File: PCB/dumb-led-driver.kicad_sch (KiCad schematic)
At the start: 17 parts, among them J1 ProgConn-SOICBite, J2 12V PWR, SW1 RESET, SW2 FLASH, U2 ESP-12F

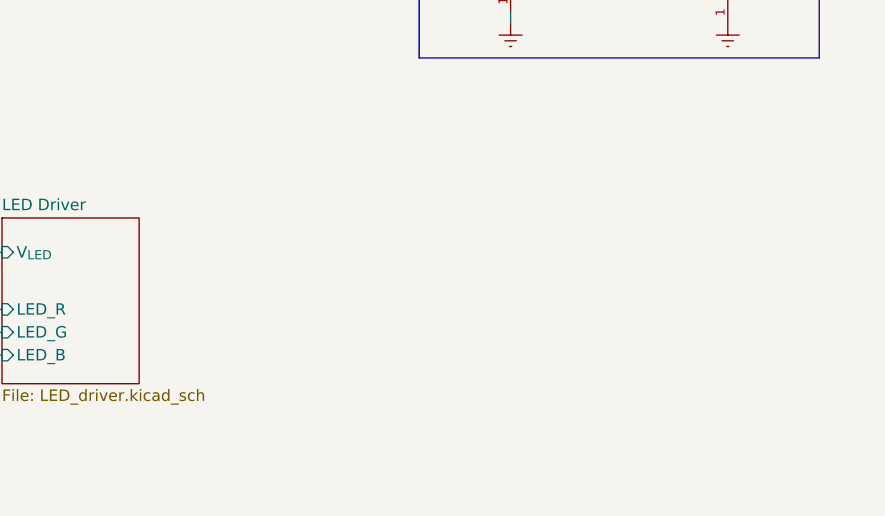
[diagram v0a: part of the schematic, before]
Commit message: fuse added to schematic. began board re-layout
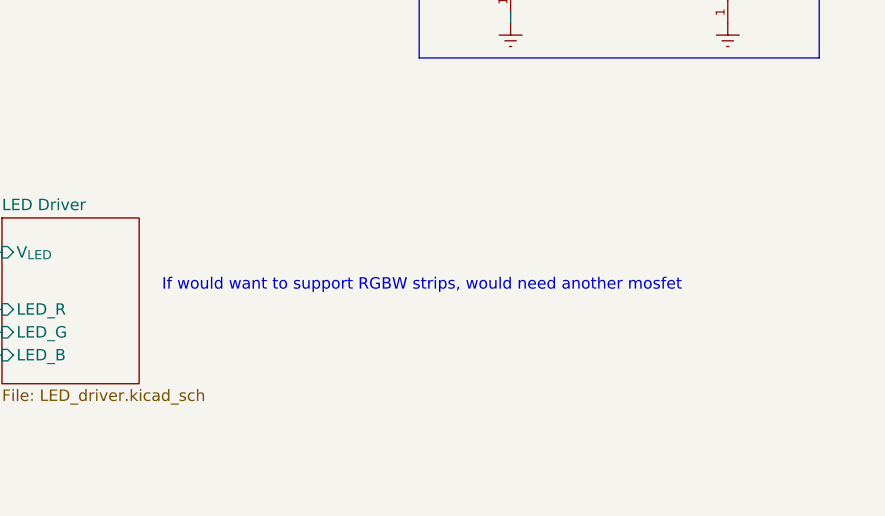
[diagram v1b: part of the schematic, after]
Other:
- note added: "If would want to support RGBW strips, would need another mosfet"
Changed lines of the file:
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@@
     (fill (type none))
+  )
+  (text "If would want to support RGBW strips, would need another mosfet"
+    (at 203.2 114.3 0)
+    (effects (font (size 1.27 1.27)) (justify left bottom))
   )
   (text "Buttons\n" (at 249.555 53.975 0)

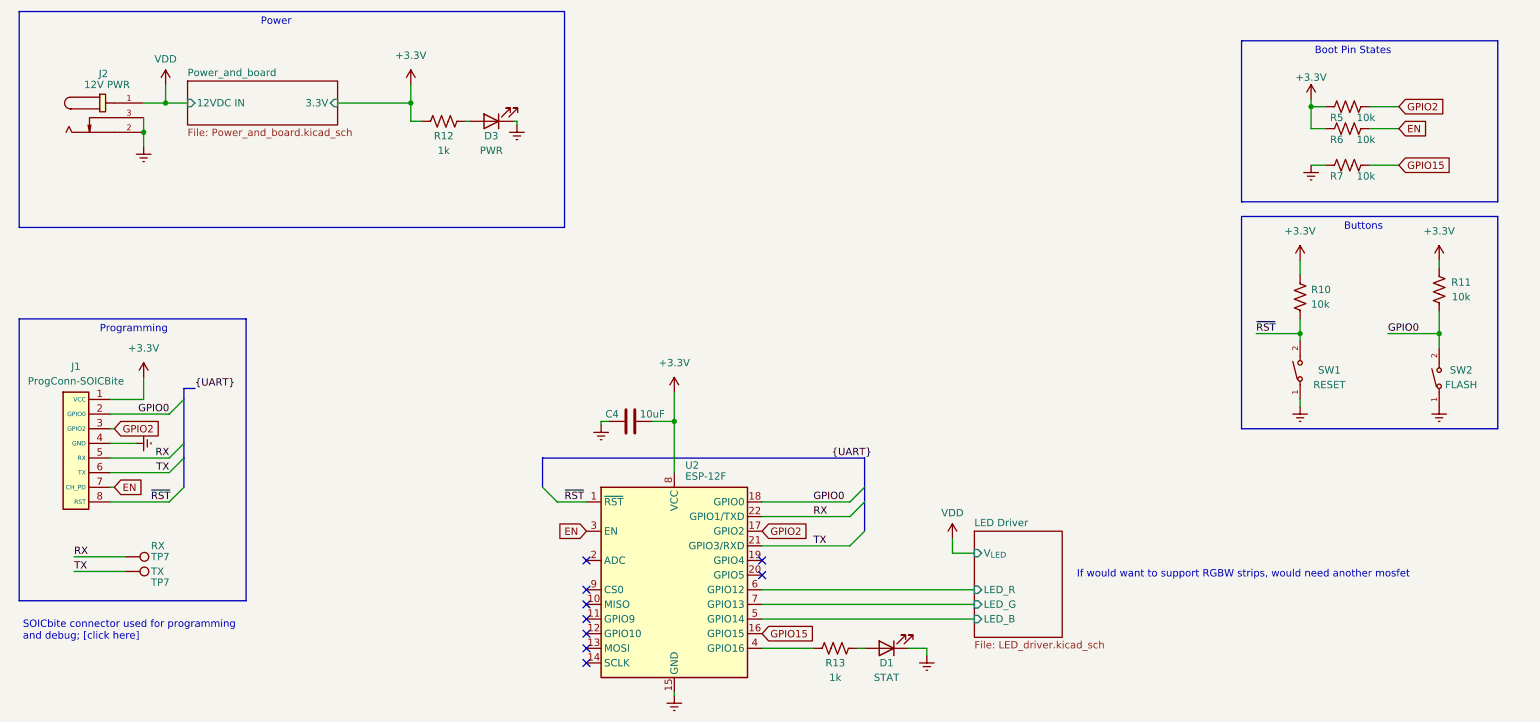
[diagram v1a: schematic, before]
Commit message: began rev2 of layout. board size will have to be increased
- will need to make compomises regarding I/O, wont be able to make both power in and out fit on same short side :(
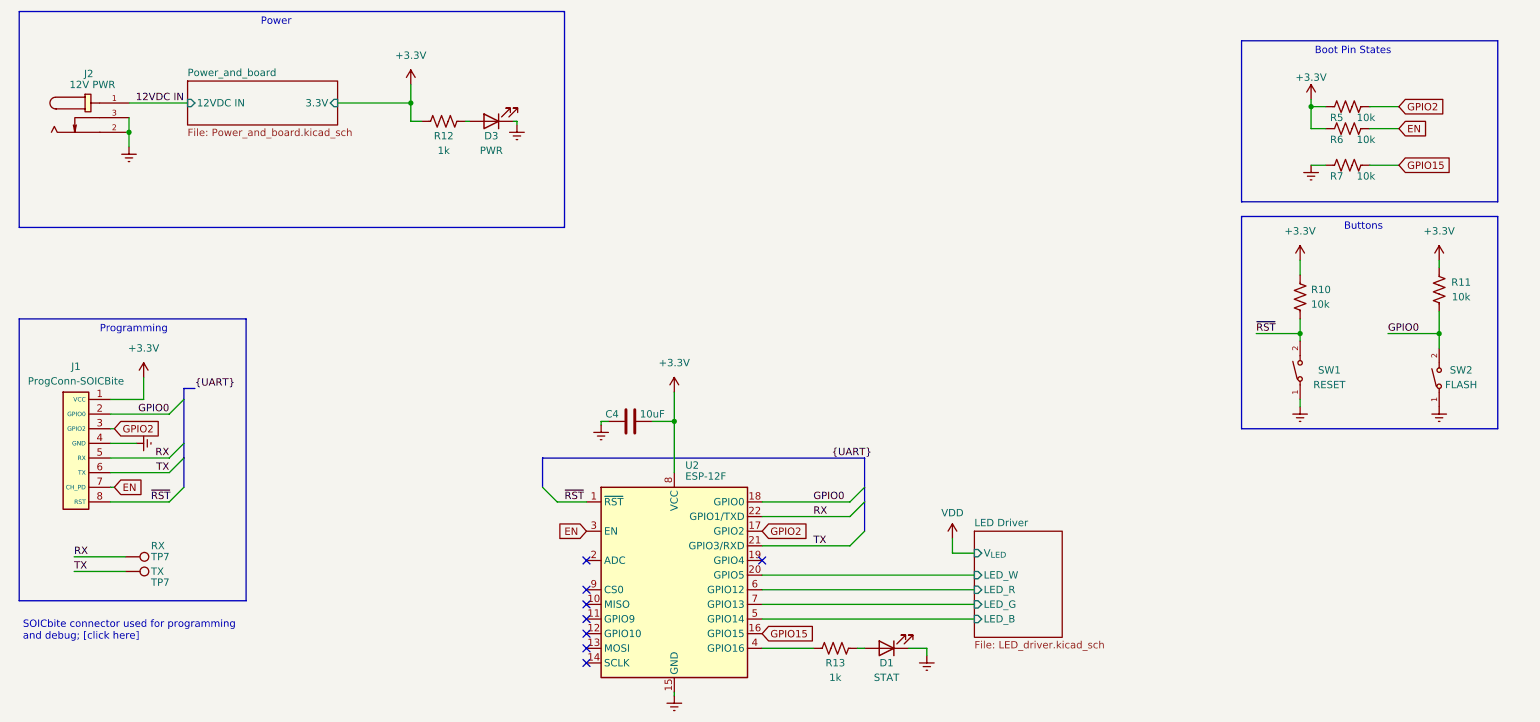
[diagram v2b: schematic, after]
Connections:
- net VDD: no longer J2.1
- net LED Driver/LED_W: now reaches U2.20 (GPIO5)
- new net 12VDC IN: J2.1
- no-connect marks 9 -> 8
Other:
- sheet LED Driver ports: added LED_W; removed none
- note removed: "If would want to support RGBW strips, would need another mosfet"
- moved on the sheet: J2
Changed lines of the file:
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@@
     (comment 1 "jacobbokor.com")
   )
-  (junction (at 45.085 31.75) (diameter 0) (color 0 0 0 0)
-  )
   (junction (at 133.35 86.995) (diameter 0) (color 0 0 0 0)
   )
@@
   (junction (at 87.63 31.75) (diameter 0) (color 0 0 0 0)
   )
-  (junction (at 41.275 36.83) (diameter 0) (color 0 0 0 0)
+  (junction (at 38.735 36.83) (diameter 0) (color 0 0 0 0)
   )
   (junction (at 243.84 32.385) (diameter 0) (color 0 0 0 0)
@@
   (no_connect (at 148.59 111.125))
   (no_connect (at 118.11 126.365))
-  (no_connect (at 148.59 113.665))
   (bus_entry (at 163.83 100.965) (size 2.54 -2.54)
     (stroke (width 0) (type default))
@@
     (stroke (width 0) (type default))
   )
-  (wire (pts (xy 45.085 31.75) (xy 48.895 31.75))
-    (stroke (width 0) (type default))
-  )
   (wire (pts (xy 133.35 86.995) (xy 133.35 95.885))
     (stroke (width 0) (type default))
@@
     (stroke (width 0) (type default))
   )
-  (wire (pts (xy 41.275 31.75) (xy 45.085 31.75))
+  (wire (pts (xy 38.735 31.75) (xy 48.895 31.75))
     (stroke (width 0) (type default))
   )
@@
     (stroke (width 0) (type default))
   )
-  (wire (pts (xy 41.275 34.29) (xy 41.275 36.83))
+  (wire (pts (xy 38.735 34.29) (xy 38.735 36.83))
     (stroke (width 0) (type default))
   )
@@
     (stroke (width 0) (type default))
   )
-  (wire (pts (xy 41.275 36.83) (xy 41.275 39.37))
+  (wire (pts (xy 38.735 36.83) (xy 38.735 39.37))
     (stroke (width 0) (type default))
   )
@@
     (stroke (width 0) (type default))
   )
+  (wire (pts (xy 148.59 113.665) (xy 185.42 113.665))
+    (stroke (width 0) (type default))
+  )
   (wire (pts (xy 97.155 34.925) (xy 97.79 34.925))
     (stroke (width 0) (type default))
@@
     (stroke (width 0) (type default))
   )
-  (wire (pts (xy 45.085 28.575) (xy 45.085 31.75))
-    (stroke (width 0) (type default))
-  )
   (bus (pts (xy 48.26 90.805) (xy 48.26 93.345))
     (stroke (width 0) (type default))
@@
     (stroke (width 0) (type default))
     (fill (type none))
-  )
-  (text "If would want to support RGBW strips, would need another mosfet"
-    (at 203.2 114.3 0)
-    (effects (font (size 1.27 1.27)) (justify left bottom))
   )
   (text "Buttons\n" (at 249.555 53.975 0)
@@
   (label "TX" (at 29.21 113.03 0) (fields_autoplaced)
     (effects (font (size 1.27 1.27)) (justify left bottom))
+  )
+  (label "12VDC IN" (at 48.26 31.75 180) (fields_autoplaced)
+    (effects (font (size 1.27 1.27)) (justify right bottom))
   )
   (label "~{RST}" (at 234.315 71.755 0) (fields_autoplaced)
@@
     )
   )
-  (symbol (lib_id "power:Earth") (at 41.275 39.37 0) (mirror y) (unit 1)
-    (in_bom yes) (on_board yes) (dnp no) (fields_autoplaced)
-    (property "Reference" "#PWR05" (at 41.275 45.72 0)
-      (effects (font (size 1.27 1.27)) hide)
-    )
-    (property "Value" "Earth" (at 41.275 43.18 0)
-      (effects (font (size 1.27 1.27)) hide)
-    )
-    (property "Footprint" "" (at 41.275 39.37 0)
-      (effects (font (size 1.27 1.27)) hide)
-    )
-    (property "Datasheet" "~" (at 41.275 39.37 0)
+  (symbol (lib_id "power:Earth") (at 38.735 39.37 0) (mirror y) (unit 1)
+    (in_bom yes) (on_board yes) (dnp no) (fields_autoplaced)
+    (property "Reference" "#PWR05" (at 38.735 45.72 0)
+      (effects (font (size 1.27 1.27)) hide)
+    )
+    (property "Value" "Earth" (at 38.735 43.18 0)
+      (effects (font (size 1.27 1.27)) hide)
+    )
+    (property "Footprint" "" (at 38.735 39.37 0)
+      (effects (font (size 1.27 1.27)) hide)
+    )
+    (property "Datasheet" "~" (at 38.735 39.37 0)
       (effects (font (size 1.27 1.27)) hide)
     )
@@
     )
   )
-  (symbol (lib_id "power:VDD") (at 45.085 28.575 0) (unit 1)
-    (in_bom yes) (on_board yes) (dnp no) (fields_autoplaced)
-    (property "Reference" "#PWR022" (at 45.085 32.385 0)
-      (effects (font (size 1.27 1.27)) hide)
-    )
-    (property "Value" "VDD" (at 45.085 24.13 0)
-      (effects (font (size 1.27 1.27)))
-    )
-    (property "Footprint" "" (at 45.085 28.575 0)
-      (effects (font (size 1.27 1.27)) hide)
-    )
-    (property "Datasheet" "" (at 45.085 28.575 0)
-      (effects (font (size 1.27 1.27)) hide)
-    )
-    (pin "1")
-    (instances
-      (project "dumb-led-driver"
-        (path "/b6358773-9a18-4eb2-bc1b-d38393a8df39"
-          (reference "#PWR022") (unit 1)
-        )
-      )
-    )
-  )
   (symbol (lib_id "Device:R_US") (at 266.065 64.135 180) (unit 1)
     (in_bom yes) (on_board yes) (dnp no)
@@
     )
   )
-  (symbol (lib_id "dc_jack_lib:DC-470-2_1GP") (at 33.655 34.29 0) (unit 1)
+  (symbol (lib_id "dc_jack_lib:DC-470-2_1GP") (at 31.115 34.29 0) (unit 1)
     (in_bom yes) (on_board yes) (dnp no)
-    (property "Reference" "J2" (at 34.29 26.67 0)
-      (effects (font (size 1.27 1.27)))
-    )
-    (property "Value" "12V PWR" (at 34.925 28.575 0)
-      (effects (font (size 1.27 1.27)))
-    )
-    (property "Footprint" "Connector_BarrelJack:BarrelJack_GCT_DCJ200-10-A_Horizontal" (at 33.655 44.45 0)
+    (property "Reference" "J2" (at 31.75 26.67 0)
+      (effects (font (size 1.27 1.27)))
+    )
+    (property "Value" "12V PWR" (at 32.385 28.575 0)
+      (effects (font (size 1.27 1.27)))
+    )
+    (property "Footprint" "Connector_BarrelJack:BarrelJack_GCT_DCJ200-10-A_Horizontal" (at 31.115 44.45 0)
       (effects (font (size 1.27 1.27) italic) hide)
     )
-    (property "Datasheet" "https://so.szlcsc.com/global.html?c=&k=C194407" (at 31.369 34.163 0)
+    (property "Datasheet" "https://so.szlcsc.com/global.html?c=&k=C194407" (at 28.829 34.163 0)
       (effects (font (size 1.27 1.27)) (justify left) hide)
     )
-    (property "LCSC" "C194407" (at 33.655 34.29 0)
-      (effects (font (size 1.27 1.27)) hide)
-    )
-    (property "Vendor" "https://www.lcsc.com/product-detail/AC-span-style-background-color-ff0-DC-span-span-style-background-color-ff0-Power-span-Connectors_GANGYUAN-DC-470-2-1GP_C194407.html" (at 33.655 34.29 0)
+    (property "LCSC" "C194407" (at 31.115 34.29 0)
+      (effects (font (size 1.27 1.27)) hide)
+    )
+    (property "Vendor" "https://www.lcsc.com/product-detail/AC-span-style-background-color-ff0-DC-span-span-style-background-color-ff0-Power-span-Connectors_GANGYUAN-DC-470-2-1GP_C194407.html" (at 31.115 34.29 0)
       (effects (font (size 1.27 1.27)) hide)
     )
@@
       (effects (font (size 1.27 1.27)) (justify left))
     )
+    (pin "LED_W" input (at 185.42 113.665 180)
+      (effects (font (size 1.27 1.27)) (justify left))
+    )
